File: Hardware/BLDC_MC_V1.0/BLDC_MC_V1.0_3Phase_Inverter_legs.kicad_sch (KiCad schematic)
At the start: 30 parts, among them Q1 BSC027N10NS5ATMA1, Q2 BSC027N10NS5ATMA1, Q3 BSC027N10NS5ATMA1, Q4 BSC027N10NS5ATMA1, Q5 BSC027N10NS5ATMA1, Q6 BSC027N10NS5ATMA1

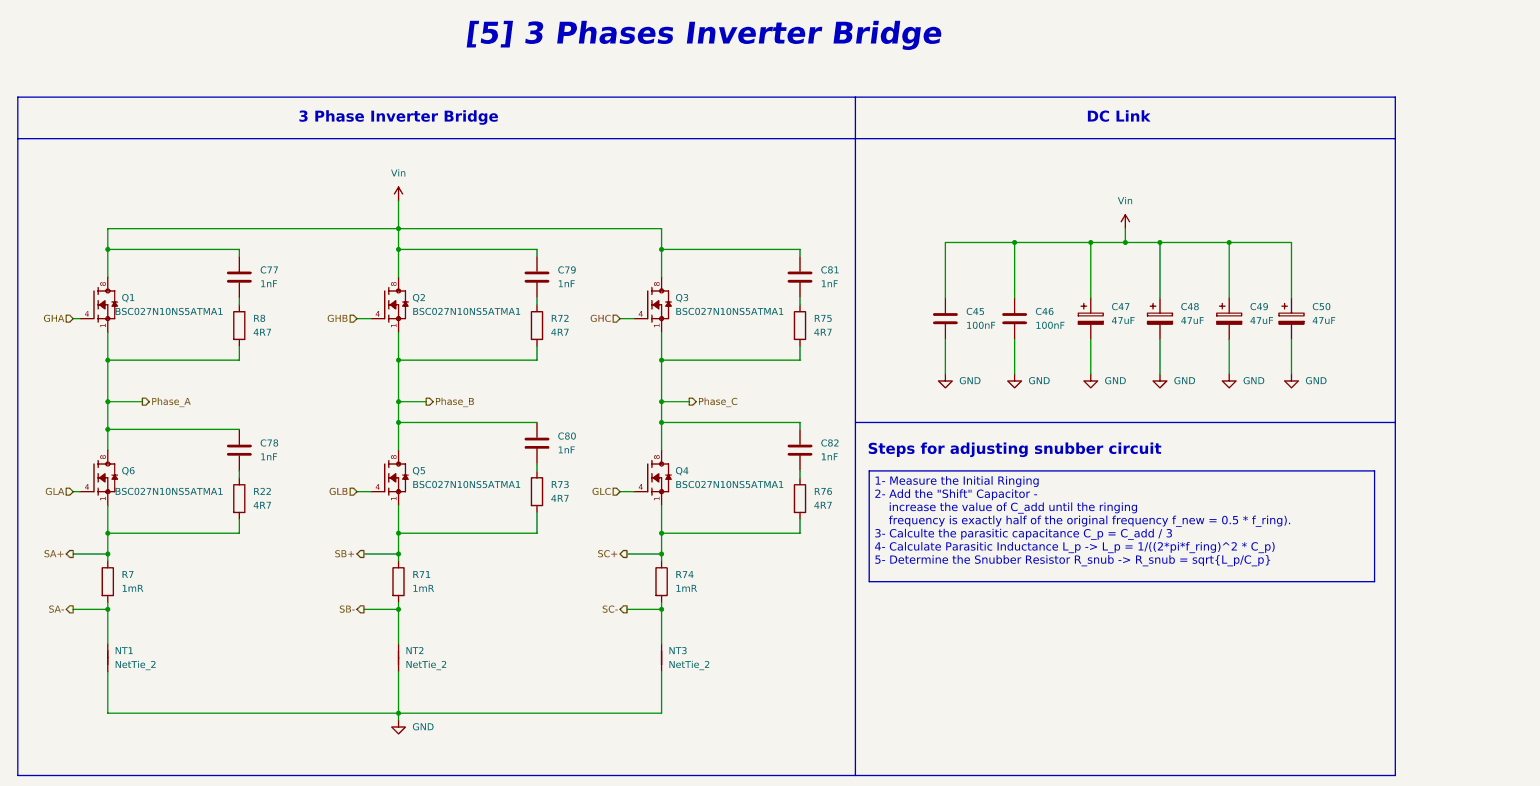
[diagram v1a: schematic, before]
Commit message: Routing the power connections and some GD signals
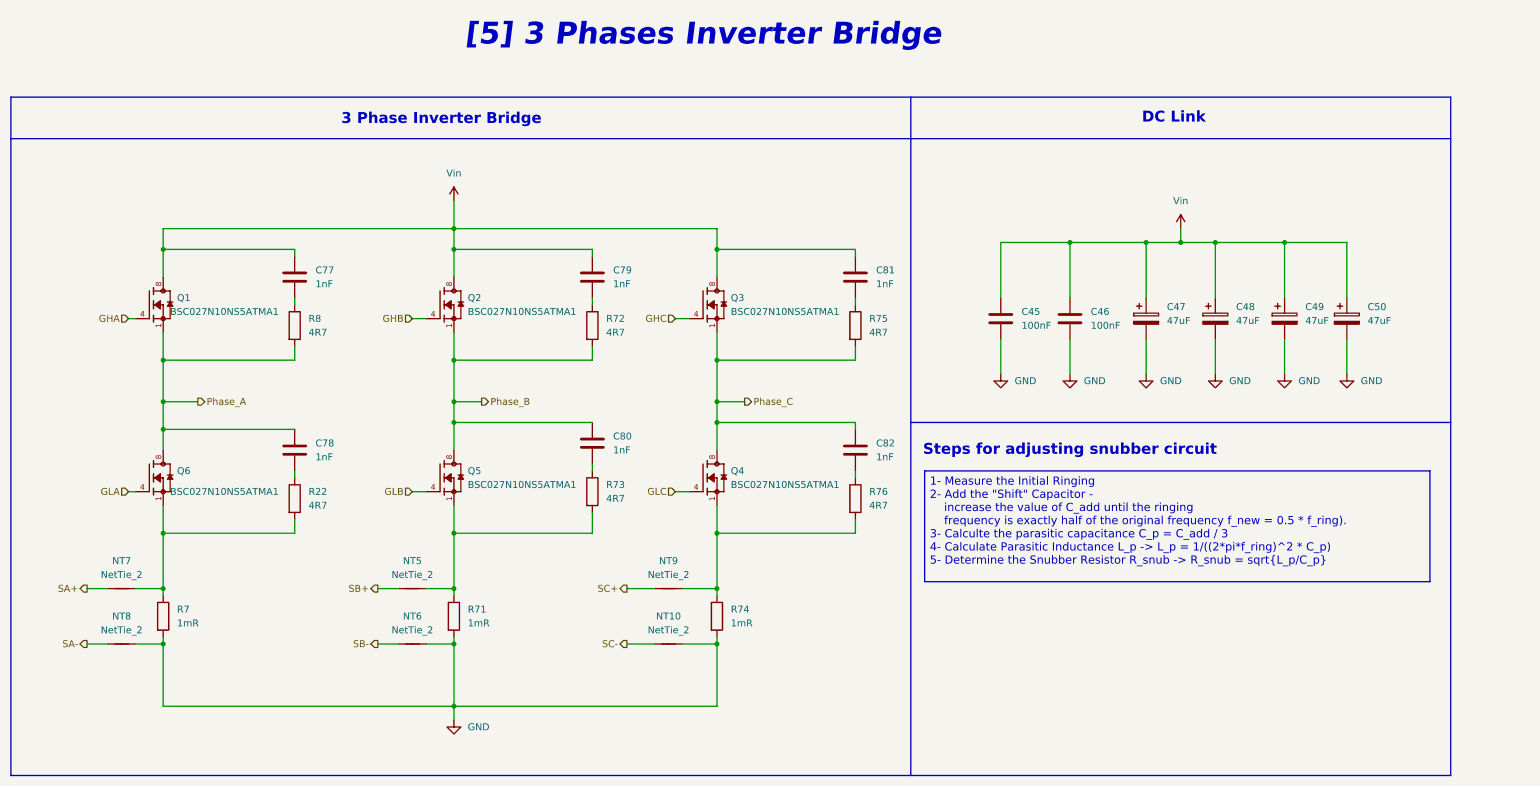
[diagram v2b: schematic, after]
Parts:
- removed NT1, NT2, NT3: NetTie_2, NetTie:NetTie-2_SMD_Pad2.0mm, symbol Device:NetTie_2
- added NT10, NT5, NT6, NT7, NT8, NT9: NetTie_2, NetTie:NetTie-2_SMD_Pad0.5mm, symbol Device:NetTie_2
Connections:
- net GND: now also R7.2, R71.2, R74.2, NT10.2, NT6.2, NT8.2
- net SA+: now also NT7.1; no longer Q6.1, Q6.2, Q6.3, R22.2, R7.1
- net SA-: now also NT8.1; no longer R7.2
- net SB+: now also NT5.1; no longer Q5.1, Q5.2, Q5.3, R71.1, R73.2
- net SB-: now also NT6.1; no longer R71.2
- net SC+: now also NT9.1; no longer Q4.1, Q4.2, Q4.3, R74.1, R76.2
- net SC-: now also NT10.1; no longer R74.2
- new net: NT5.2, Q5.1, Q5.2, Q5.3, R71.1, R73.2
- new net: NT9.2, Q4.1, Q4.2, Q4.3, R74.1, R76.2
- new net: NT7.2, Q6.1, Q6.2, Q6.3, R22.2, R7.1
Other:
- moved on the sheet: C45, C46, C47, C48, C49, C50, C77, C78, C79, C80, C81, C82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

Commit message: Edited the label of the Schematic sheets
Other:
- company: (none) -> Ahmed Aboeita
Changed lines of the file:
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@@
 	(title_block
 		(title "${Project_Name}")
-		(date "2026-01-07")
-		(rev "V1")
+		(date "2026-08-17")
+		(rev "V1.0")
+		(company "Ahmed Aboeita")
+		(comment 1 "8-Layer High-TG180 PCB with Kelvin Current Sensing")
+		(comment 2 "Power Stage: 3-Phase Inverter with Active Reverse Polarity & E-Fuse OCP")
+		(comment 3 "Core MCU: STM32G431RBT6 (FOC & CORDIC Processing, 100 kHz PWM)")
+		(comment 4 "Stackup & Sensing: System Ratings: 100V DC Bus | 50A Continuous | T_A = 125 degrees  ")
 	)
 	(rectangle
